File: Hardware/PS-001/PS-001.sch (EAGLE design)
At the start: 115 parts, among them J1 10144517-042802LF, J2 10144518-041802LF, J3 10144517-042802LF, J4 10144518-041802LF, J6 2X5_0.05_SWD, Q1 STD15P6F6AG, Q2 DMP3018SFVQ-13, Q3 DMP3018SFVQ-13, U2 MAX16935CAUES/V+, U3 MAX16935CAUES/V+, U4 INA186A2IDCKT, U5 INA2180A4IDGKR, U6 NCV8170AXV330T2G, U7 ATA6561-GAQW-N, U8 LM2902DT, U9 LM2902DT

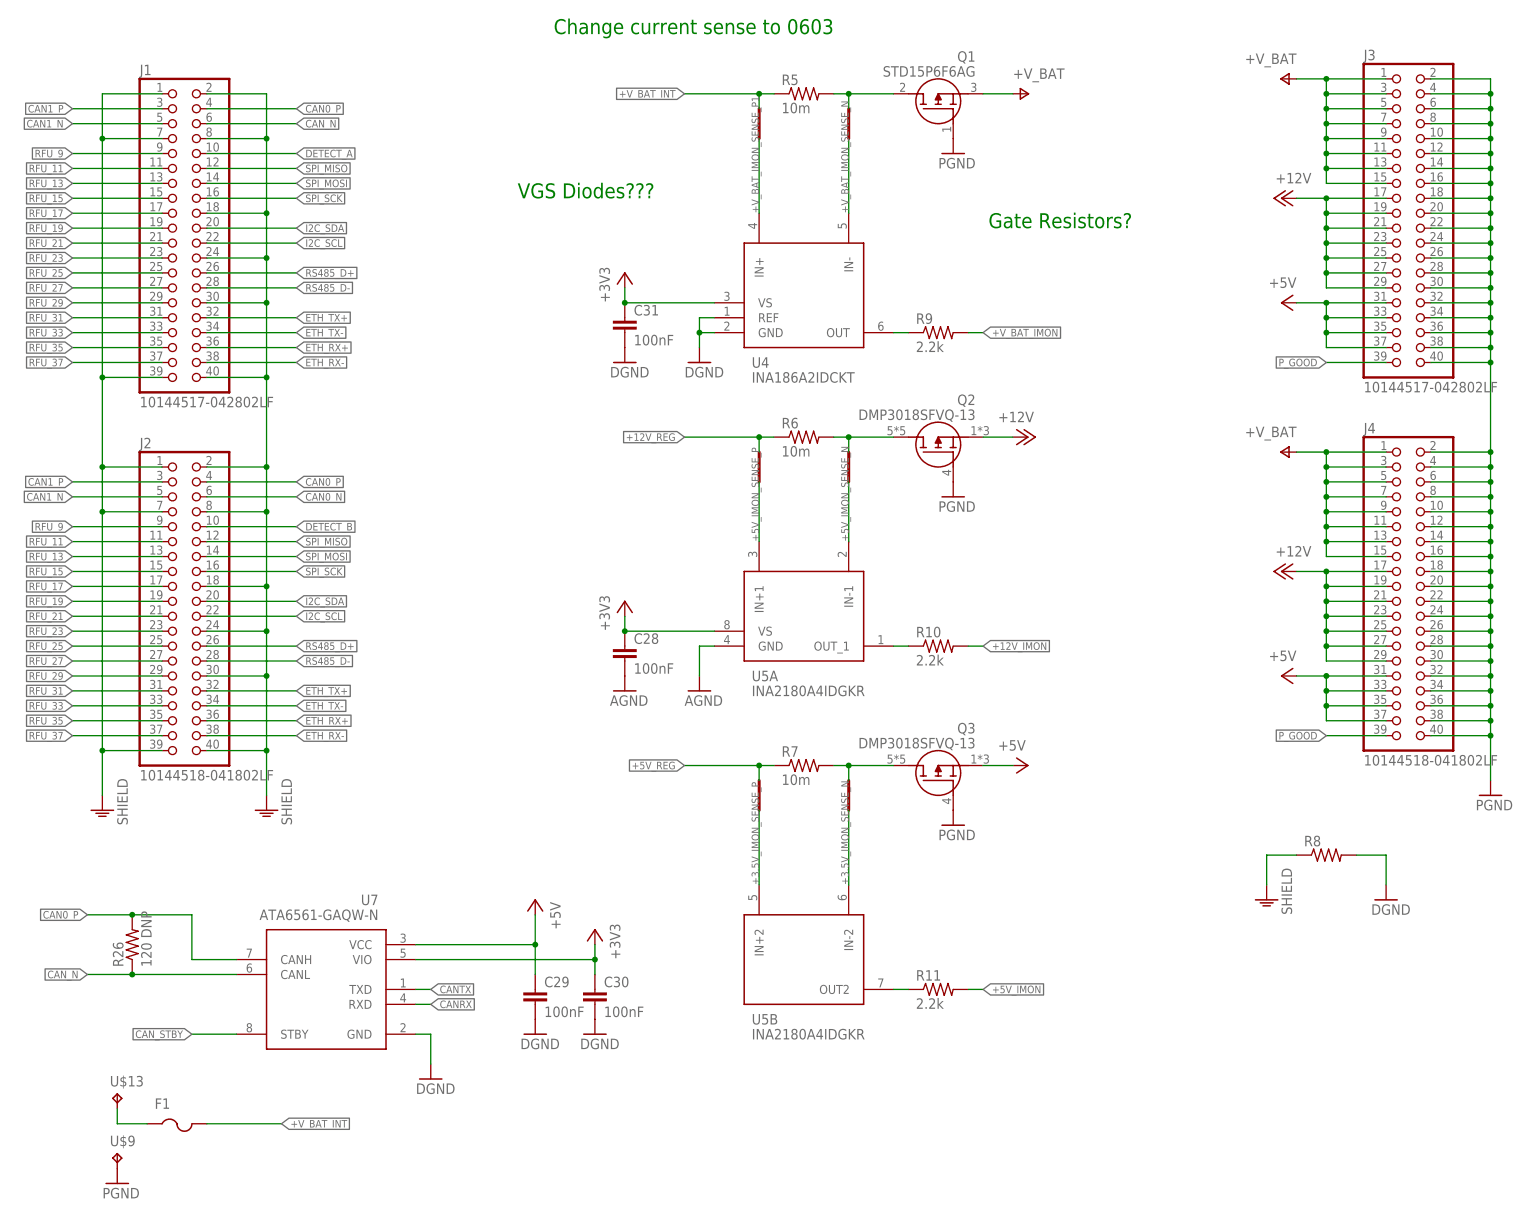
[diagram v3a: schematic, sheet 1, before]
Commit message: fixed supply ORing
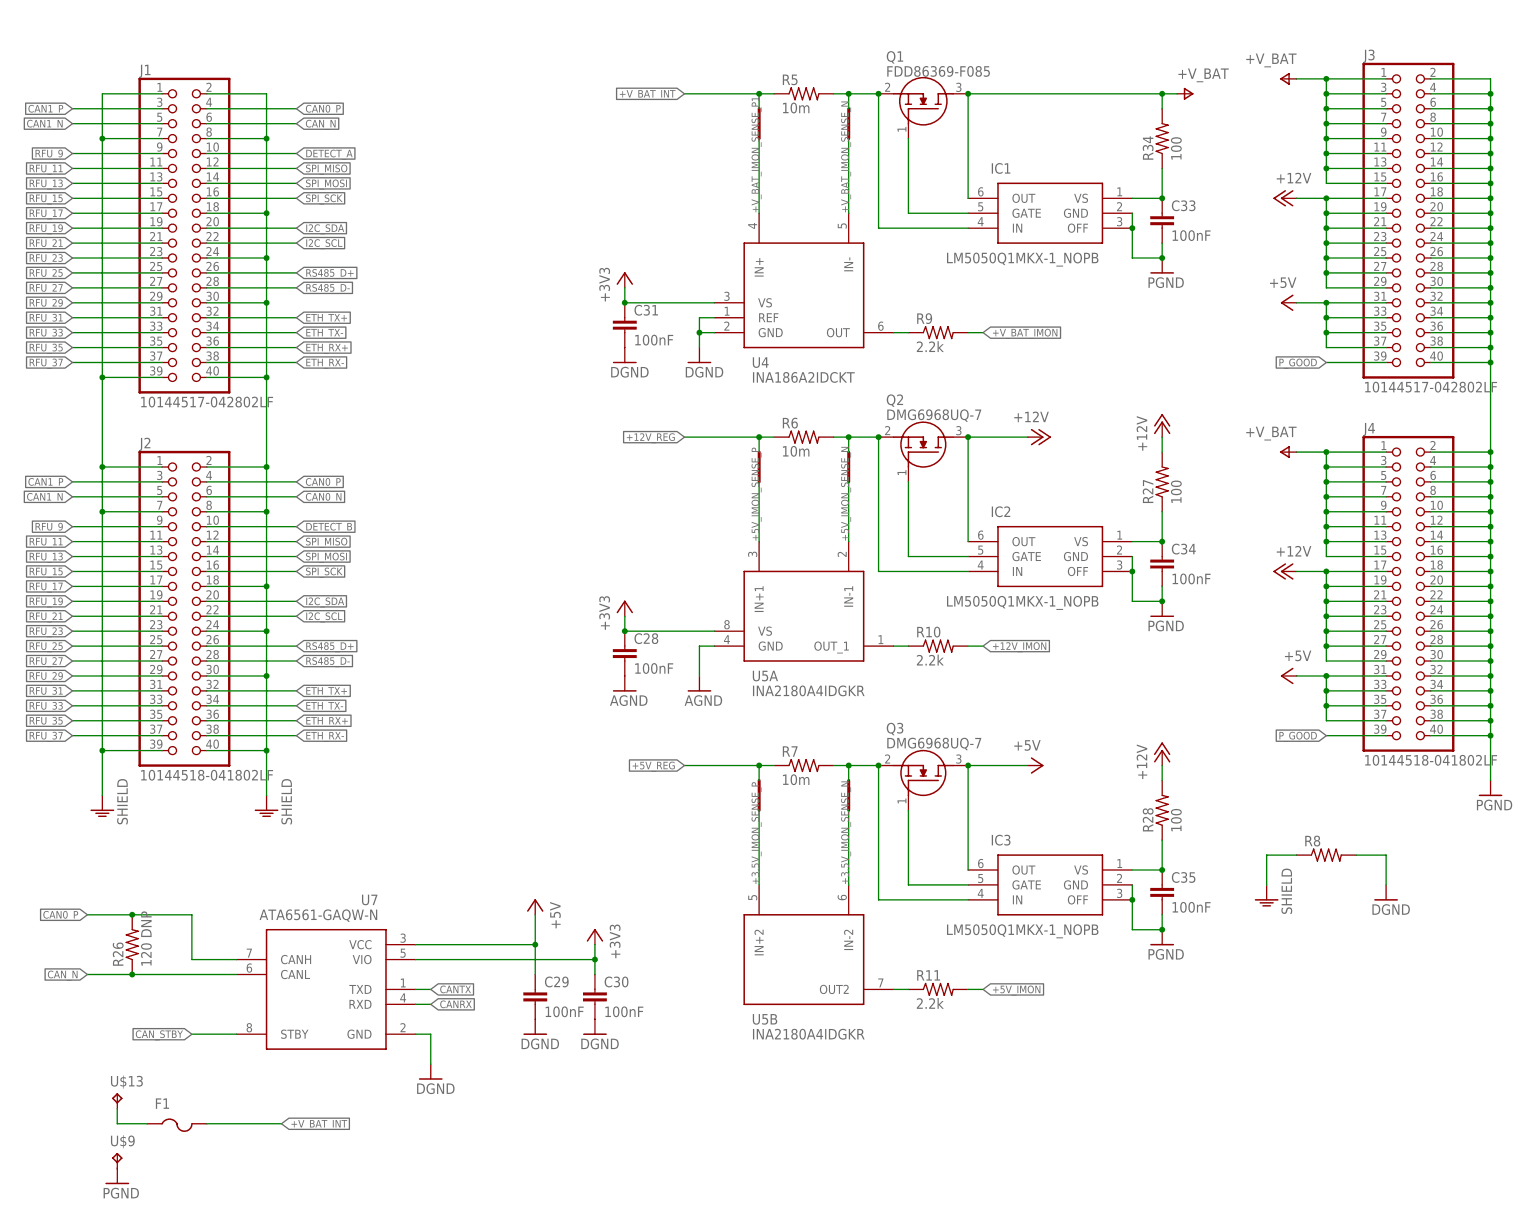
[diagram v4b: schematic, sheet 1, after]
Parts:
- removed C42, C43: 100nF, rcl:C-EUC0402
- removed U8, U9: LM2902DT, SamacSys Managed:LM2902DT
- added C33, C34, C35: 100nF, rcl:C-EUC0402
- added IC1, IC2, IC3: LM5050Q1MKX-1_NOPB, SamacSys_Parts:LM5050Q1MKX-1_NOPB
- added R34: 100, rcl:R-US_R0402
- Q1: value STD15P6F6AG -> FDD86369-F085; device SamacSys Managed:STD15P6F6AG -> SamacSys_Parts:FDD86369-F085
- Q2, Q3: value DMP3018SFVQ-13 -> DMG6968UQ-7; device SamacSys Managed:DMP3018SFVQ-13 -> SamacSys_Parts:DMG6968UQ-7
- R27: value 5.6k -> 100
- R28: value 2.2k -> 100
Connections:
- removed net +12V: J3.17, J3.19, J3.21, J3.23, J3.25, J3.27, J3.29, J4.17, J4.19, J4.21, J4.23, J4.25, J4.27, J4.29, Q2.S
- removed net +3.5V: R14.2
- removed net +3.5V_INT_VMON: U$60G$2.PA03, U9G$1.-IN, U9G$1.OUT
- removed net +3.5V_VMON: U$60G$2.PB09, U9G$2.-IN, U9G$2.OUT
- removed net +5V_FB: R27.1, R28.2, U3.FB
- removed net N$15: C39.1, R18.1, R19.2, U9G$4.+IN
- removed net N$23: C37.1, R14.1, R15.2, U9G$2.+IN
- removed net N$24: C41.1, R22.1, R23.2, U8G$2.+IN
- removed net N$27: U8G$3.-IN, U8G$3.OUT
- new net +12V_INT_VMON: C38.1, R16.1, R17.2, U$60G$2.PA04
- new net +12V_VMON: C39.1, R18.1, R19.2, U$60G$2.PA05
- new net N$20: IC2.GATE, Q2.G
- new net N$22: C34.1, IC2.VS, R27.1
- net +12V_FB: now also U2.FB
- net +3.3V_INT_VMON: now also C44.1, R24.1, R25.2; no longer U8G$4.-IN, U8G$4.OUT
- net +3V3: no longer C42.1, C43.1, U8G$5.AVCC, U9G$5.AVCC
- net +5V: now also IC2.OUT, IC3.OUT, J3.17, J3.19, J3.21, J3.23, J3.25, J3.27, J3.29, J4.17, J4.19, J4.21, J4.23, J4.25, J4.27, J4.29, Q2.D, Q3.D, R14.2, R27.2, R28.2; no longer Q3.S
- net +5V_INT_VMON: now also C36.1, R12.1, R13.2, U$60G$2.PA03; no longer U$60G$2.PA04, U9G$3.-IN, U9G$3.OUT
- net +5V_REG: no longer R27.2
- net +5V_VMON: now also C37.1, R14.1, R15.2, U$60G$2.PB09; no longer U$60G$2.PA05, U9G$4.-IN, U9G$4.OUT
- net +V_BAT: now also IC1.OUT, Q1.D, R34.2; no longer Q1.S
- net +V_BAT_INT_VMON: now also C40.1, R20.1, R21.2; no longer U8G$1.-IN, U8G$1.OUT
- net +V_BAT_VMON: now also C41.1, R22.1, R23.2; no longer U8G$2.-IN, U8G$2.OUT
- net AGND: no longer C42.2, C43.2, U8G$5.AGND, U9G$5.AGND
- net GND2: no longer R28.1
- net N$11: now also IC2.IN, Q2.S; no longer Q2.D
- net N$12: now also IC3.IN, Q3.S; no longer Q3.D
- net N$13: now also IC1.GATE, Q1.G; no longer C38.1, R16.1, R17.2, U9G$3.+IN
- net N$14: now also C33.1, IC1.VS, R34.1; no longer C36.1, R12.1, R13.2, U9G$1.+IN
- net N$19: now also IC1.IN, Q1.S; no longer Q1.D
- net N$25: now also IC3.GATE, Q3.G; no longer C44.1, R24.1, R25.2, U8G$3.+IN, U8G$4.+IN
- net N$26: now also C35.1, IC3.VS, R28.1; no longer C40.1, R20.1, R21.2, U8G$1.+IN
- net PGND: now also C33.2, C34.2, C35.2, IC1.GND, IC1.OFF, IC2.GND, IC2.OFF, IC3.GND, IC3.OFF; no longer Q1.G, Q2.G, Q3.G
- net VBIAS_U2: no longer U2.FB
- net VBIAS_U3: now also U3.FB
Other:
- note removed: "Change current sense to 0603"
- note removed: "Gate Resistors?"
- note removed: "VGS Diodes???"
- note removed: "replace FB voltage drivider with fixed output for 5V?"
- note removed: "should we just get rid of the voltage following opamps? they aren't adding much value, but taking up lots of board space"
- moved on the sheet: C51, C52, Q1

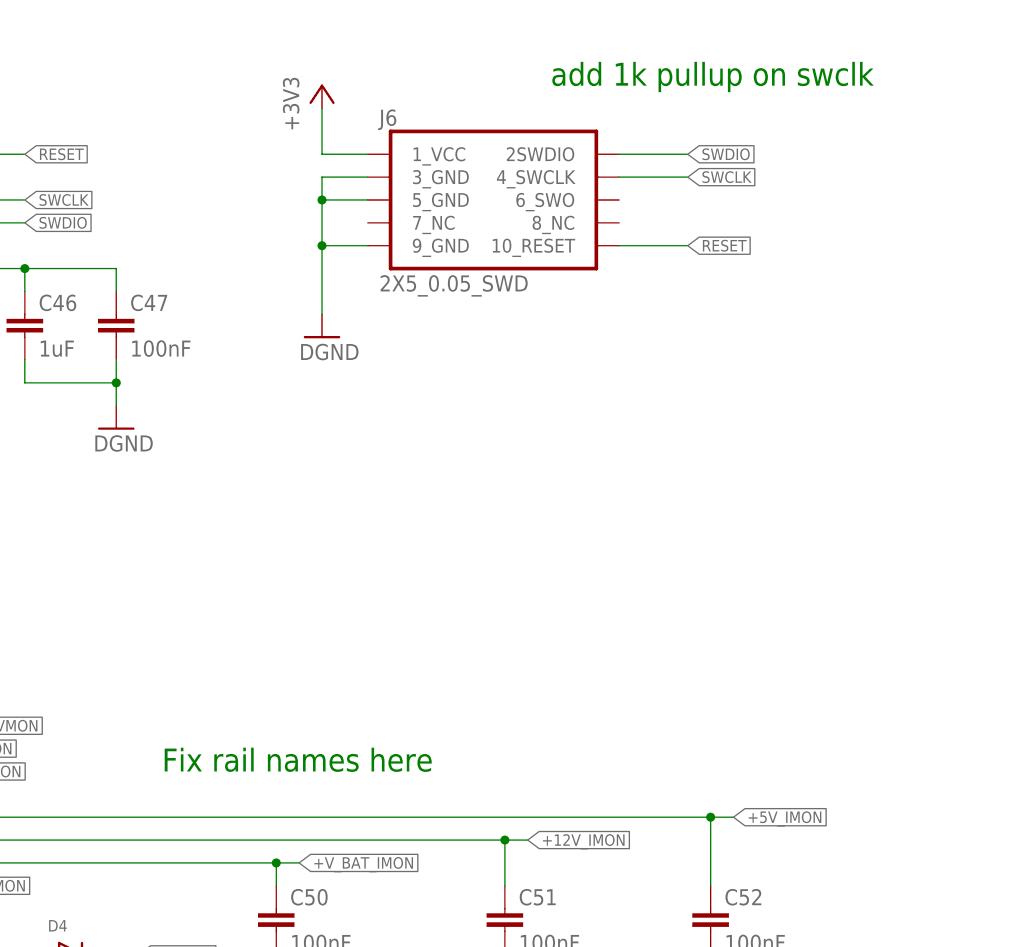
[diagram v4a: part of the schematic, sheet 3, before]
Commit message: added pullup and swdclk and changed some cap packages
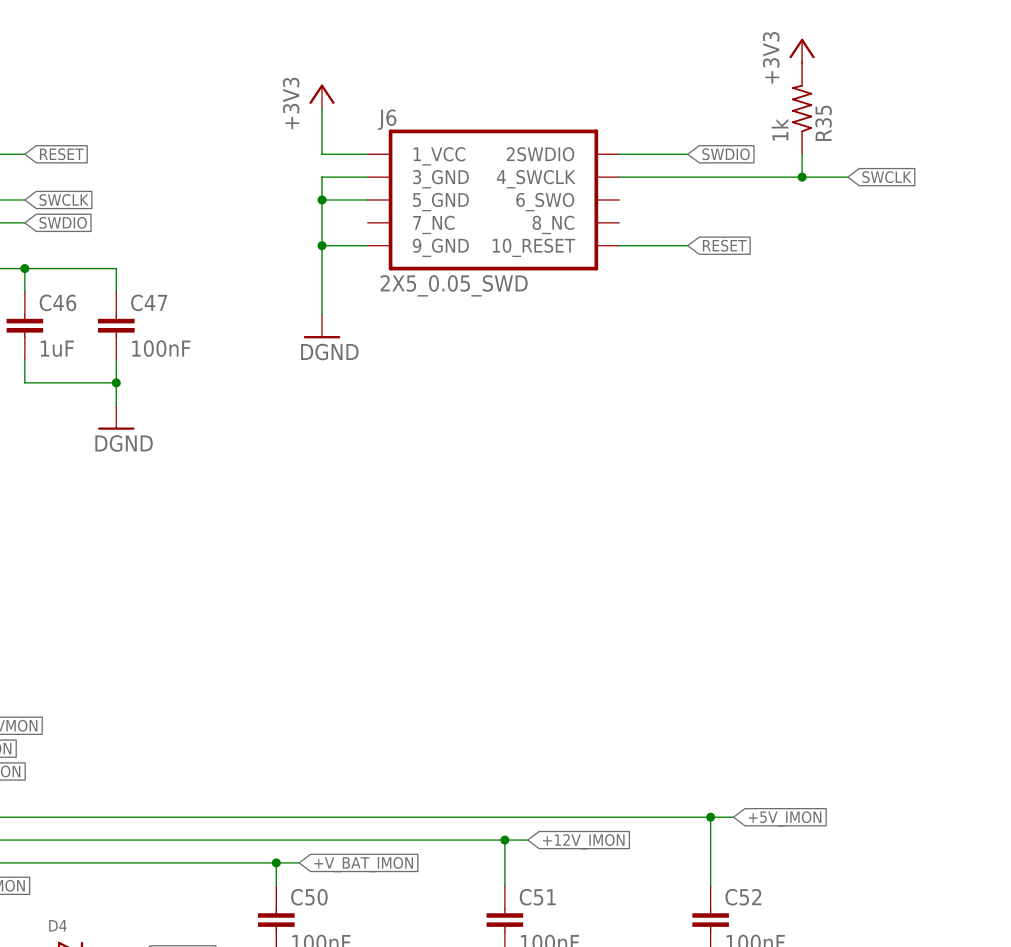
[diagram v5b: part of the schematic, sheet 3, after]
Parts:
- added R35: 1k, rcl:R-US_R0402
- C1, C2: value 1uF -> 10uF; device rcl:C-EUC0603 -> rcl:C-EUC0805
- C15, C27: device rcl:C-EUC0805 -> rcl:C-EUC0402
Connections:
- net +3V3: now also R35.2
- net SWCLK: now also R35.1
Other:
- note removed: "Fix rail names here"
- note removed: "Use internal power good here for en?"
- note removed: "add 1k pullup on swclk"
- note removed: "more bulk"
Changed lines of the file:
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@@
 <part name="+3V4" library="supply1" library_urn="urn:adsk.eagle:library:371" deviceset="+3V3" device=""/>
 <part name="U6" library="SamacSys_Parts" deviceset="NCV8170AXV330T2G" device=""/>
-<part name="C1" library="rcl" library_urn="urn:adsk.eagle:library:334" deviceset="C-EU" device="C0603" package3d_urn="urn:adsk.eagle:package:23616/2" value="1uF"/>
-<part name="C2" library="rcl" library_urn="urn:adsk.eagle:library:334" deviceset="C-EU" device="C0603" package3d_urn="urn:adsk.eagle:package:23616/2" value="1uF"/>
+<part name="C1" library="rcl" library_urn="urn:adsk.eagle:library:334" deviceset="C-EU" device="C0805" package3d_urn="urn:adsk.eagle:package:23617/2" value="10uF"/>
+<part name="C2" library="rcl" library_urn="urn:adsk.eagle:library:334" deviceset="C-EU" device="C0805" package3d_urn="urn:adsk.eagle:package:23617/2" value="10uF"/>
 <part name="U$2" library="Supply" deviceset="+V_BAT" device=""/>
 <part name="C3" library="rcl" library_urn="urn:adsk.eagle:library:334" deviceset="C-EU" device="C0603" package3d_urn="urn:adsk.eagle:package:23616/2" value="100nF"/>
@@
 <part name="R1" library="rcl" library_urn="urn:adsk.eagle:library:334" deviceset="R-US_" device="R0603" package3d_urn="urn:adsk.eagle:package:23555/2" value="63.4k"/>
 <part name="R2" library="rcl" library_urn="urn:adsk.eagle:library:334" deviceset="R-US_" device="R0603" package3d_urn="urn:adsk.eagle:package:23555/2" value="40.2k"/>
-<part name="C15" library="rcl" library_urn="urn:adsk.eagle:library:334" deviceset="C-EU" device="C0805" package3d_urn="urn:adsk.eagle:package:23617/2" value="1uF"/>
+<part name="C15" library="rcl" library_urn="urn:adsk.eagle:library:334" deviceset="C-EU" device="C0402" package3d_urn="urn:adsk.eagle:package:23626/2" value="1uF"/>
 <part name="D1" library="SamacSys_Parts" deviceset="RBR3MM60ATFTR" device=""/>
 <part name="Q1" library="SamacSys_Parts" deviceset="FDD86369-F085" device=""/>
@@
 <part name="R3" library="rcl" library_urn="urn:adsk.eagle:library:334" deviceset="R-US_" device="R0603" package3d_urn="urn:adsk.eagle:package:23555/2" value="63.4k"/>
 <part name="R4" library="rcl" library_urn="urn:adsk.eagle:library:334" deviceset="R-US_" device="R0603" package3d_urn="urn:adsk.eagle:package:23555/2" value="40.2k"/>
-<part name="C27" library="rcl" library_urn="urn:adsk.eagle:library:334" deviceset="C-EU" device="C0805" package3d_urn="urn:adsk.eagle:package:23617/2" value="1uF"/>
+<part name="C27" library="rcl" library_urn="urn:adsk.eagle:library:334" deviceset="C-EU" device="C0402" package3d_urn="urn:adsk.eagle:package:23626/2" value="1uF"/>
 <part name="D2" library="SamacSys_Parts" deviceset="RBR3MM60ATFTR" device=""/>
 <part name="U5" library="SamacSys_Parts" deviceset="INA2180A2IDGKR" device="" value="INA2180A4IDGKR"/>
@@
 <part name="P+3" library="supply1" library_urn="urn:adsk.eagle:library:371" deviceset="+5V" device=""/>
 <part name="P+8" library="supply1" library_urn="urn:adsk.eagle:library:371" deviceset="+5V" device=""/>
+<part name="R35" library="rcl" library_urn="urn:adsk.eagle:library:334" deviceset="R-US_" device="R0402" package3d_urn="urn:adsk.eagle:package:23547/3" value="1k"/>
+<part name="+3V3" library="supply1" library_urn="urn:adsk.eagle:library:371" deviceset="+3V3" device=""/>
 </parts>
 <sheets>
@@
 <sheet>
 <plain>
-<text x="99.06" y="66.04" size="2.54" layer="91">Use internal power good here for en?</text>
 <text x="264.16" y="139.7" size="2.54" layer="91" rot="MR0">recalculate voltage divider for FB</text>
-<text x="157.48" y="50.8" size="2.54" layer="91">more bulk</text>
 <text x="205.74" y="182.88" size="2.54" layer="91">simulate output ringing??</text>
 </plain>
@@
 <sheet>
 <plain>
-<text x="106.68" y="116.84" size="2.54" layer="91" ratio="10">Fix rail names here</text>
-<text x="149.86" y="193.04" size="2.54" layer="91" ratio="10">add 1k pullup on swclk</text>
 </plain>
 <instances>
@@
 <attribute name="VALUE" x="165.1" y="91.44" size="1.778" layer="96"/>
 </instance>
+<instance part="R35" gate="G$1" x="177.8" y="190.5" smashed="yes" rot="MR90">
+<attribute name="NAME" x="179.2986" y="186.69" size="1.778" layer="95" rot="MR90"/>
+<attribute name="VALUE" x="174.498" y="186.69" size="1.778" layer="96" rot="MR90"/>
+</instance>
+<instance part="+3V3" gate="G$1" x="177.8" y="198.12" smashed="yes">
+<attribute name="VALUE" x="175.26" y="193.04" size="1.778" layer="96" rot="R90"/>
+</instance>
 </instances>
 <busses>
@@
 <net name="SWCLK" class="0">
 <segment>
-<wire x1="157.48" y1="182.88" x2="165.1" y2="182.88" width="0.1524" layer="91"/>
-<label x="165.1" y="182.88" size="1.27" layer="95" xref="yes"/>
+<wire x1="157.48" y1="182.88" x2="177.8" y2="182.88" width="0.1524" layer="91"/>
+<label x="182.88" y="182.88" size="1.27" layer="95" xref="yes"/>
 <pinref part="J6" gate="J" pin="4_SWCLK"/>
+<pinref part="R35" gate="G$1" pin="1"/>
+<wire x1="177.8" y1="182.88" x2="182.88" y2="182.88" width="0.1524" layer="91"/>
+<wire x1="177.8" y1="185.42" x2="177.8" y2="182.88" width="0.1524" layer="91"/>
+<junction x="177.8" y="182.88"/>
 </segment>
 <segment>
@@
 <junction x="10.16" y="182.88"/>
 </segment>
-</net>
+<segment>
+<pinref part="R35" gate="G$1" pin="2"/>
+<pinref part="+3V3" gate="G$1" pin="+3V3"/>
+</segment>
+</net>

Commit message: updates to ps-001
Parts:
- removed R31: (no value), rcl:R-US_R0402
- removed SH7, SH8: SHORTT8, shorts:SHORTT8
- C32: value 100nF -> 10uF
- C48, C49: device rcl:C-EUC0805 -> rcl:C-EUC0402
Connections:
- removed net GND1: C13.2, C14.2, C15.2, R2.1, R33.1, SH7.P$1, U2.AGND
- removed net GND2: C25.2, C26.2, C27.2, R4.1, SH8.P$1, U3.AGND
- new net +12V: IC2.OUT, J3.17, J3.19, J3.21, J3.23, J3.25, J3.27, J3.29, J4.17, J4.19, J4.21, J4.23, J4.25, J4.27, J4.29, Q2.D, R18.2, R27.2, R28.2
- net +12V_IMON: now also C52.1, U$60G$2.PA06; no longer C51.1, U$60G$2.PA07
- net +5V: no longer IC2.OUT, J3.17, J3.19, J3.21, J3.23, J3.25, J3.27, J3.29, J4.17, J4.19, J4.21, J4.23, J4.25, J4.27, J4.29, Q2.D, R18.2, R27.2, R28.2
- net +5V_IMON: now also C51.1, U$60G$2.PA07; no longer C52.1, U$60G$2.PA06
- net AGND: no longer C36.2, C37.2, C38.2, C39.2, C40.2, C41.2, C44.2, R13.1, R15.1, R17.1, R19.1, R21.1, R23.1, R25.1, R31.2
- net CAN0_N: now also R26.1, U7.CANL
- net CAN_N: no longer R26.1, U7.CANL
- net DGND: now also C13.2, C14.2, C15.2, C25.2, C26.2, C27.2, C36.2, C37.2, C38.2, C39.2, C40.2, C41.2, C44.2, R13.1, R15.1, R17.1, R19.1, R2.1, R21.1, R23.1, R25.1, R33.1, R4.1, U2.AGND, U3.AGND; no longer R31.1
- net PGND: no longer SH7.P$2, SH8.P$2
